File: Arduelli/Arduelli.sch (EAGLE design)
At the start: 2 parts, among them J3 DF12-ELLI-RECEPTABLE-BOTTOM, U1 ARDUINO_SHIELDLONGPADS

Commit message: Preliminary version of Arduelli
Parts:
- removed J3: DF12-ELLI-RECEPTABLE-BOTTOM, ELL-i-Connectors:DF12-ELLI-RECEPTABLE-BOTTOM
- added C1: 10uF, ELL-i-Passives:C0603
- added C10: 33n, ELL-i-Passives:C0402
- added C11, C2, C4, C5, C6, C7, C8, C9: 0.1uF, ELL-i-Passives:C0402
- added C16: 47u, ELL-i-Passives:CPOL6032
- added C17: 47pF, ELL-i-Passives:C0805
- added C39: 100nF, ELL-i-Passives:C0805
- added D1, D4: BAT60J, ell-i:BAT60J
- added D3: MBR120, tinycircuits:AS-ITM-00111
- added FB1, FB2, FB3, FB4: (no value), ELL-i-Passives:FB1206
- added J1, J6: 47346-0001, ELL-i-Connectors:MICRO-USB
- added J2: DF12-ELLI-RECEPTABLE-BOTTOM, ELL-i-Connectors:DF12-ELLI-RECEPTABLE-BOTTOM
- added J4: FTDI-SER-6-PP, ELL-i-Connectors:FTDI-SER-6-PP
- added J5: JTAG_PROG, ELL-i-Connectors:JTAG_PROG
- added Q1: NTZD3152P, ELL-i-DiscreteSemi:NTZD3152P
- added Q2: 2N7002PT, tinycircuits:AS-ITM-00110
- added R1, R11, R12, R13, R2, R20, R21, R22, R3: 100k, ELL-i-Passives:R0402
- added R10, R18, R19, R9: 330, ELL-i-Passives:R0402
- added R14, R15, R16, R17, R4, R6, R7, R8: 24 1%, ELL-i-Passives:R0402
- added R33: 1k5, ELL-i-Passives:R0402
- added R5: 10k, ELL-i-Passives:R0402
- added S1, S3: Push button switch, SparkFun-Electromechanical:SWITCH-MOMENTARY-2SMD
- added S2: EVQQ2/P0, ell-i:EVQQ2/P0
- added SJ16: CLOSED, SparkFun-Passives:SOLDERJUMPERTRACE
- added SJ3, SJ4: OPEN, SparkFun-Passives:SOLDERJUMPERNO
- added SW1, SW2, SW3: (no value), SparkFun-Electromechanical:SW_DIP-2-SMT-HALFSIZE
- added TP2, TP3, TP4: TEST_POINT-5021, ELL-i-Passives:TEST_POINT-5021
- added U2: STM32F103RB, ELL-i-DigitalIC:STM32F103RB
- added U3, U4: ADUM4160BRWZ, ELL-i-PowerIC:ADUM4160BRWZ
- added U5: NCP1117, ell-i:NCP1117
- added X1, X2: XMK-8788K5-BX1X, ELL-i-Connectors:POE-TP-SHIELDED-LEDS
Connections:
- removed net RX+: J3.RX+
- removed net RX-: J3.RX-
- removed net TX+: J3.TX+
- removed net TX-: J3.TX-
- removed net VBAT: J3.VBATT
- removed net VDDA: J3.AREF
- new net +5V0: C16.+, TP2.P$1, U5.OUT, U5.TAB
- new net -RTS: C10.2, SW1.3
- new net AGND: C11.1, C5.1, C6.1, C9.1, S1.2, S3.2, U3.GND2, U3.GND2_2, U4.GND2, U4.GND2_2, X1LED2.C, X2LED2.C
- new net AREF: J2.AREF
- new net BOOT0TX: J4.TXD, R5.1, SW1.4
- new net CTS: J4.-CTS
- new net D14: J2.IO5
- new net D15: J2.MOSI
- new net D16: J2.IO3
- new net D17: J2.IO8
- new net D18: J2.IO2
- new net DDD+: R8.2
- new net DDD-: R7.2
- new net DPIN: U3.PIN
- new net DSPD: U3.SPD
- new net DSPU: U3.SPU
- new net DUD+: J1.D+, R6.1
- new net DUD-: J1.D-, R4.1
- new net DVBUS1: C2.2, FB1.1, R10.2, U3.VBUS1
- new net DVBUS2: R9.1
- new net DVDD1: C4.2, U3.PDEN, U3.VDD1
- new net ETH_INT: J2.ETH_INT/TX+
- new net ETH_RX+: J2.RX+
- new net ETH_RX-: J2.RX-
- new net GND: C1.2, C2.1, C4.1, C7.1, C8.1, FB2.1, FB4.1, J1.P1, J1.P2, J1.P3, J1.P4, J1.P5, J1.P6, J5.3, J5.5, J5.9, J6.P1, J6.P2, J6.P3, J6.P4, J6.P5, J6.P6, Q2.S, R1.1, U3.GND1, U3.GND1_2, U4.GND1, U4.GND1_2, X1LED1.C, X2LED1.C
- new net GNDA: R3.1
- new net HDD+: R17.2, SJ4.2
- new net HDD-: R16.2, SJ3.2
- new net HPIN: U4.PIN
- new net HSPD: U4.SPD
- new net HSPU: U4.SPU
- new net HUD+: J6.D+, R15.1
- new net HUD-: J6.D-, R14.1
- new net HVBUS1: C7.2, R19.2, U4.VBUS1
- new net HVBUS2: FB3.1, R18.1
- new net HVDD1: C8.2, U4.PDEN, U4.VDD1
- new net N$1: FB1.2, J1.VBUS
- new net N$15: C1.1
- new net N$16: R7.1, U3.DD-
- new net N$17: R8.1, U3.DD+
- new net N$18: R11.1
- new net N$19: R12.1
- new net N$2: D3.C, Q1.D2
- new net N$20: R11.2
- new net N$21: R12.2
- new net N$22: R13.1
- new net N$23: R13.2, S1.1
- new net N$24: FB3.2, J6.VBUS
- new net N$25: FB4.2, J6.GND
- new net N$26: R14.2, U4.UD-
- new net N$27: R15.2, U4.UD+
- new net N$28: R16.1, U4.DD-
- new net N$29: R17.1, U4.DD+
- new net N$3: FB2.2, J1.GND
- new net N$30: R18.2, X2LED2.A
- new net N$31: R19.1, X2LED1.A
- new net N$32: R20.1
- new net N$33: R21.1
- new net N$34: R20.2
- new net N$35: C17.1, C39.1, TP3.P$1, U5.IN
- new net N$36: R9.2, X1LED2.A
- new net N$37: R21.2
- new net N$38: R10.1, X1LED1.A
- new net N$39: R22.1
- new net N$4: U2PA.PA11
- new net N$40: R22.2, S3.1
- new net N$5: U2PA.PA12
- new net N$58: C16.-, C17.2, C39.2, TP4.P$1, U5.GND
- new net N$6: R4.2, U3.UD-
- new net N$7: R6.2, U3.UD+
- new net N$8: Q1.G2, Q2.D, R2.1
- new net RSV2: J2.RSV2
- new net RTS: C10.1, J4.-RTS
- new net RX: R5.2, SW3.1, U2PA.PA10
- new net TCLK: J5.4, U2PA.PA5-ADC_IN5
- new net TDI: J5.8, U2PA.PA3-ADC_IN3
- new net TDO: J5.6, U2PA.PA6-ADC_IN6
- new net TMS: J5.2, U2PA.PA4-ADC_IN4
- new net TX: J4.RXD, SW3.2, U2PA.PA9
- new net USB_POWER: Q1.D1, R1.2
- new net VBATT: J2.VBATT
- new net VCC: Q1.S1, Q1.S2, R2.2
- new net VCC-IN: D4.A, J4.VCC
- new net VCCIO: J2.VCC(IO), SJ16.1
- net +3V3: now also C11.2, C5.2, C6.2, C9.2, D1.C, D4.C, J2.3.3V@48, J2.3.3V@6, J2.ETH_MUX, J5.1, SJ16.2, U3.VBUS2, U3.VDD2, U4.VBUS2, U4.VDD2; no longer J3.3.3V@48, J3.3.3V@6, J3.VCC(IO)
- net +5V: now also D3.A, J2.5V, Q1.G1, Q2.G, R3.2; no longer J3.5V
- net A0: now also J2.AD0; no longer J3.AD0
- net A1: now also J2.AD1; no longer J3.AD1
- net A2: now also J2.AD2; no longer J3.AD2
- net A3: now also J2.AD3; no longer J3.AD3
- net A4: now also J2.SDA; no longer J3.SDA
- net A5: now also J2.SCL; no longer J3.SCL
- net BOOT0: now also J2.BOOT0, R33.2, SW1.1, U2PD_CTL.BOOT0; no longer J3.RSV2
- net D0: now also SW3.3, U1.RX; no longer J3.IO0
- net D1: now also SW3.4, U1.TX; no longer J3.IO1
- net D10: now also J2.SS; no longer J3.SS
- net D11: now also J2.SCK; no longer J3.MOSI
- net D12: now also J2.MISO; no longer J3.MISO
- net D13: no longer J3.SCK
- net D2: now also J2.TX1/IO1; no longer J3.IO2
- net D3: now also SJ3.1; no longer J3.IO3
- net D4: now also SJ4.1; no longer J3.IO4
- net D5: now also J2.RX1/IO0; no longer J3.IO5
- net D6: now also J2.IO6; no longer J3.IO6
- net D7: now also J2.IO4; no longer J3.IO7
- net D8: now also J2.IO7; no longer J3.IO8
- net D9: now also J2.IO9; no longer J3.IO9
- net E0: now also J2.E0; no longer J3.E0
- net E1: now also J2.E1; no longer J3.E1
- net E10: now also J2.E10; no longer J3.E10
- net E11: now also J2.E11; no longer J3.E11
- net E12: now also J2.SDA2; no longer J3.SDA2
- net E13: now also J2.SCL2; no longer J3.SCL2
- net E14: now also J2.SS2/CANRX; no longer J3.SS2/CANRX
- net E15: now also J2.MOSI2; no longer J3.MOSI2
- net E16: now also J2.MISO2; no longer J3.MISO2
- net E17: now also J2.SCK2/CANTX; no longer J3.SCK2/CANTX
- net E18: now also J2.RX2/E18; no longer J3.E18
- net E19: now also J2.TX2/E19; no longer J3.E19
- net E2: now also J2.E2; no longer J3.E2
- net E3: now also J2.E3; no longer J3.E3
- net E4: now also J2.E4; no longer J3.E4
- net E5: now also J2.E5; no longer J3.E5
- net E6: now also J2.E6; no longer J3.E6
- net E7: now also J2.E7; no longer J3.E7
- net E8: now also J2.E8; no longer J3.E8
- net E9: now also J2.E9; no longer J3.E9
- net ETH_SS: now also J2.ETH_SS/TX-; no longer J3.ETH_SPI_SS
- net GNDI: now also J2.GND@12, J2.GND@14, J2.GND@46, J4.GND, R33.1, S2.P; no longer J3.ETH_MUX, J3.GND@12, J3.GND@14, J3.GND@46
- net NRES: now also D1.A, J2.-RESET, J5.10, S2.S, SW1.2, U2PD_CTL.NRST; no longer J3.-RESET
- net RSV0: now also J2.RSV0; no longer J3.RSV0
- net RSV1: now also J2.RSV1; no longer J3.RSV1
- net VIN: now also J2.VIN; no longer J3.VIN
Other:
- note added: "Connect close to the package"
- note added: "IO expansion bus"
- note added: "LED indicators for power"
- note added: "Low ESR"
- note added: "POE POWER"
- note added: "Power arbitration"
- note added: "RESET LOGIC"
- note added: "Simulate device disconnect"
- note added: "UGND"
- note added: "USB POWER"
- note added: "USB debug interface"
- note added: "USB2.0 speeds - Pulled up USB1.0 speeds - Pulled down Default - Pulled up"
- note added: "VCC of Ardueli"
- note added: "V_USB"
- moved on the sheet: U1

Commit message: Arduelli with the crystal and other connections
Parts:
- removed SW2: (no value), SparkFun-Electromechanical:SW_DIP-2-SMT-HALFSIZE
- added C12, C3: 18pF, ELL-i-Passives:C0402
- added Q3: 8MHz, SparkFun-FreqCtrl:CRYSTAL_WITH_GND
- added R23: 330E, ELL-i-Passives:R0402
- added SW4: (no value), SparkFun-Electromechanical:SW_DIP-8-SMT-HALFSIZE
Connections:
- removed net N$35: C17.1, C39.1, TP3.P$1, U5.IN
- removed net N$58: C16.-, C17.2, C39.2, TP4.P$1, U5.GND
- new net LDO_GND: C16.-, C17.2, C39.2, SW4.5, SW4.7, TP4.P$1, U5.GND
- new net LDO_IN: C17.1, C39.1, SW4.6, SW4.8, TP3.P$1, U5.IN
- new net N$10: C12.2, Q3.C2, R23.2
- new net N$9: C3.2, Q3.C1, U2PD_CTL.PD0
- net +3V3: now also U2PB.PB4, U2PWR.VBAT, U2PWR.VDD1, U2PWR.VDD2, U2PWR.VDD3, U2PWR.VDD4, U2PWR.VDDA
- net DDD+: now also U2PA.PA12
- net DDD-: now also U2PA.PA11
- net DVBUS1: now also SW4.9
- net GND: now also C12.1, C3.1, SW4.10, U2PWR.VSS1, U2PWR.VSS2, U2PWR.VSS3, U2PWR.VSS4, U2PWR.VSSA
- net GNDI: now also SW4.12
- net HVBUS2: now also SW4.11
- net N$4: now also Q3.GND@1, Q3.GND@2; no longer U2PA.PA11
- net N$5: now also R23.1, U2PD_CTL.PD1; no longer U2PA.PA12
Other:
- moved on the sheet: C1, C10, D1, D3, D4, J4, Q1, Q2, R1, R2, R3, R33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

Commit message: Fixed the RJ45 issue in layout. Minor fixes.
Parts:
- removed Q3: 8MHz, SparkFun-FreqCtrl:CRYSTAL_WITH_GND
- removed R23: 330E, ELL-i-Passives:R0402
- removed X1, X2: XMK-8788K5-BX1X, ELL-i-Connectors:POE-TP-SHIELDED-LEDS
- added D2, D5, D6, D7: GREEN, SparkFun-LED:LED-GREEN0603
- added Y1: 8MHz, SparkFun-FreqCtrl:CRYSTALTXC-7A
- C12, C3: value 18pF -> 16pF
- R10, R18, R19, R9: value 330 -> (none)
- U2: value STM32F103RB -> STM32F103RBT; device ELL-i-DigitalIC:STM32F103RB -> ELL-i-DigitalIC:STM32F103RBT
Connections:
- removed net N$30: R18.2, X2LED2.A
- removed net N$31: R19.1, X2LED1.A
- removed net N$36: R9.2, X1LED2.A
- removed net N$38: R10.1, X1LED1.A
- new net N$11: D2.C, R9.1
- new net N$12: D5.C, R10.1
- net AGND: now also R10.2, R19.2; no longer X1LED2.C, X2LED2.C
- net DVBUS1: now also D2.A; no longer R10.2
- net DVBUS2: now also D5.A; no longer R9.1
- net GND: now also R18.2, R9.2; no longer X1LED1.C, X2LED1.C
- net HVBUS1: now also D6.A; no longer R19.2
- net HVBUS2: now also D7.A; no longer R18.1
- net N$10: now also U2PD_CTL.PD1; no longer Q3.C2, R23.2
- net N$4: now also D6.C, R18.1; no longer Q3.GND@1, Q3.GND@2
- net N$5: now also D7.C, R19.1; no longer R23.1, U2PD_CTL.PD1
- net N$9: no longer Q3.C1
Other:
- moved on the sheet: R10, R18, R19, R9

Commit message: Added pins, nets for Arduino header. Minor fixes.
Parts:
- R10, R18, R19, R9: value (none) -> 150R
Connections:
- removed net D14: J2.IO5
- removed net D15: J2.MOSI
- removed net D16: J2.IO3
- removed net D17: J2.IO8
- removed net D18: J2.IO2
- net +3V3: now also U1.3.3V
- net +5V: now also U1.5V
- net A0: now also U1.A0
- net A1: now also U1.A1
- net A2: now also U1.A2
- net A3: now also U1.A3
- net A4: now also U1.A4
- net A5: now also U1.A5
- net AREF: now also U1.AREF
- net D0: now also J2.RX1/IO0
- net D1: now also J2.TX1/IO1
- net D10: now also U1.*D10
- net D11: now also J2.MOSI, U1.*D11; no longer J2.SCK
- net D12: now also U1.D12
- net D13: now also J2.SCK
- net D2: now also J2.IO2, U1.D2; no longer J2.TX1/IO1
- net D3: now also J2.IO3, U1.*D3
- net D4: now also J2.IO4, U1.D4
- net D5: now also J2.IO5, U1.*D5; no longer J2.RX1/IO0
- net D6: now also U1.*D6
- net D7: now also J2.IO7, U1.D7; no longer J2.IO4
- net D8: now also J2.IO8, U1.D8; no longer J2.IO7
- net D9: now also U1.*D9
- net GND: now also U1.GND@0, U1.GND@1, U1.GND@2
- net NRES: now also U1.RES
- net VIN: now also U1.VIN

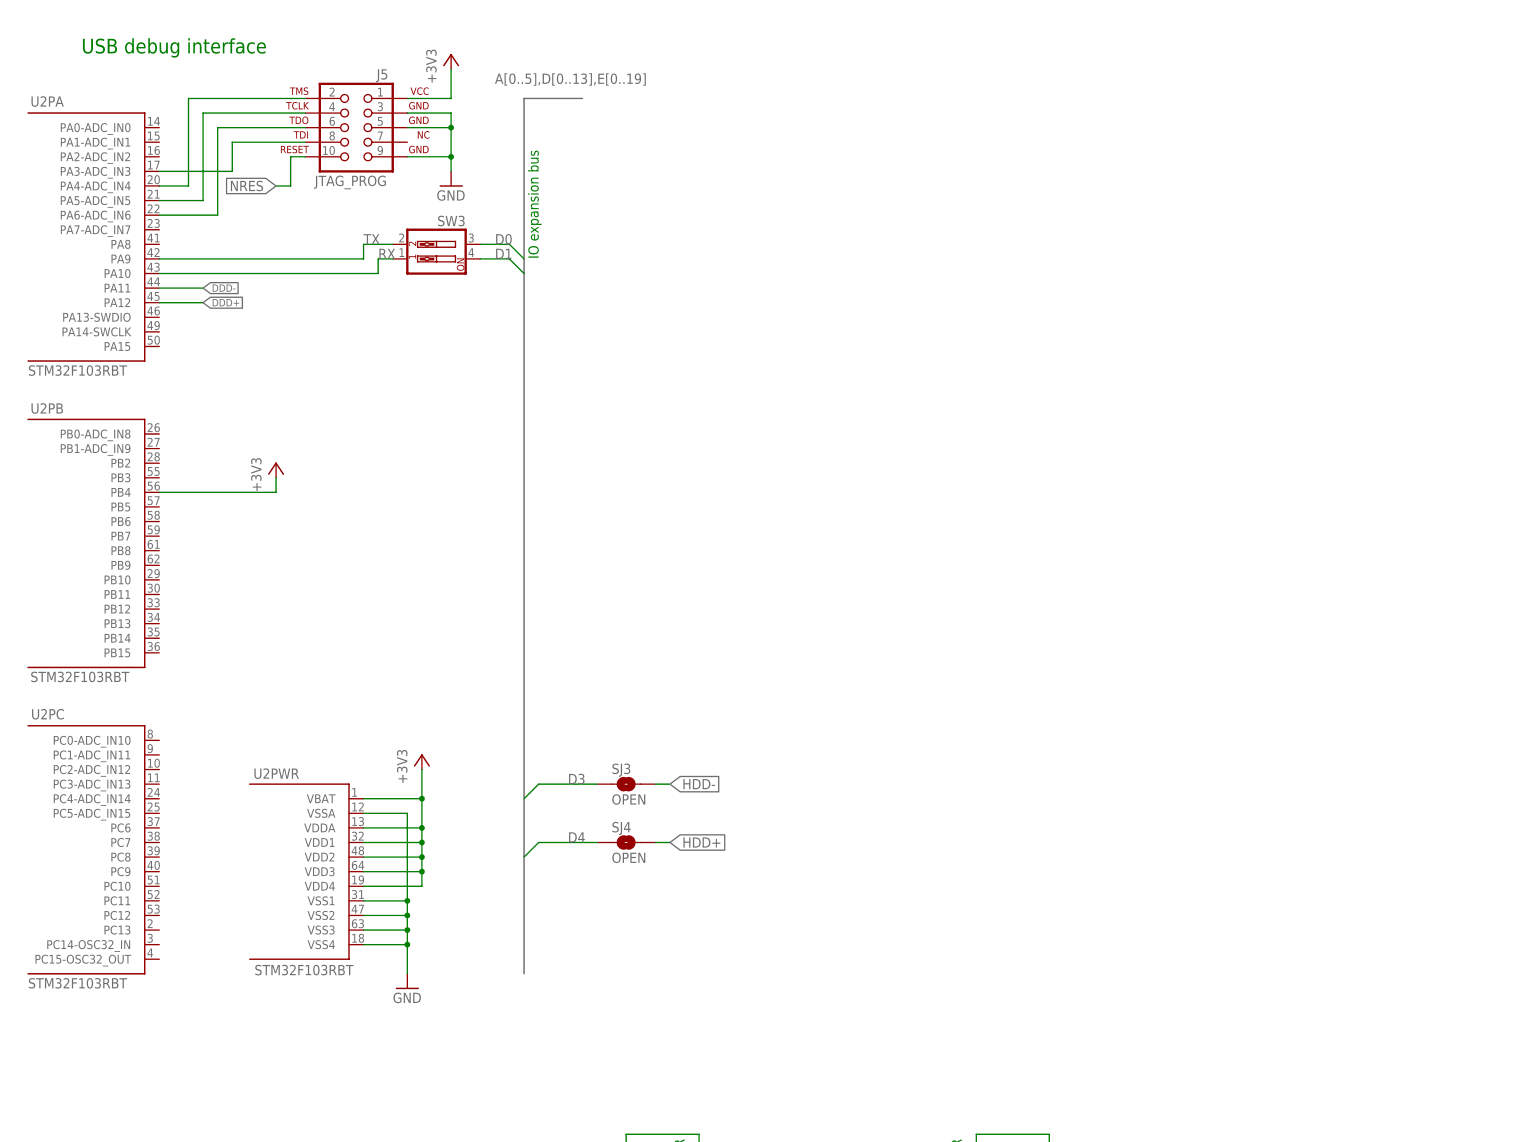
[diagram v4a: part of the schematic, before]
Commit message: Adding connections to the ELL-i bus. Other fixes.
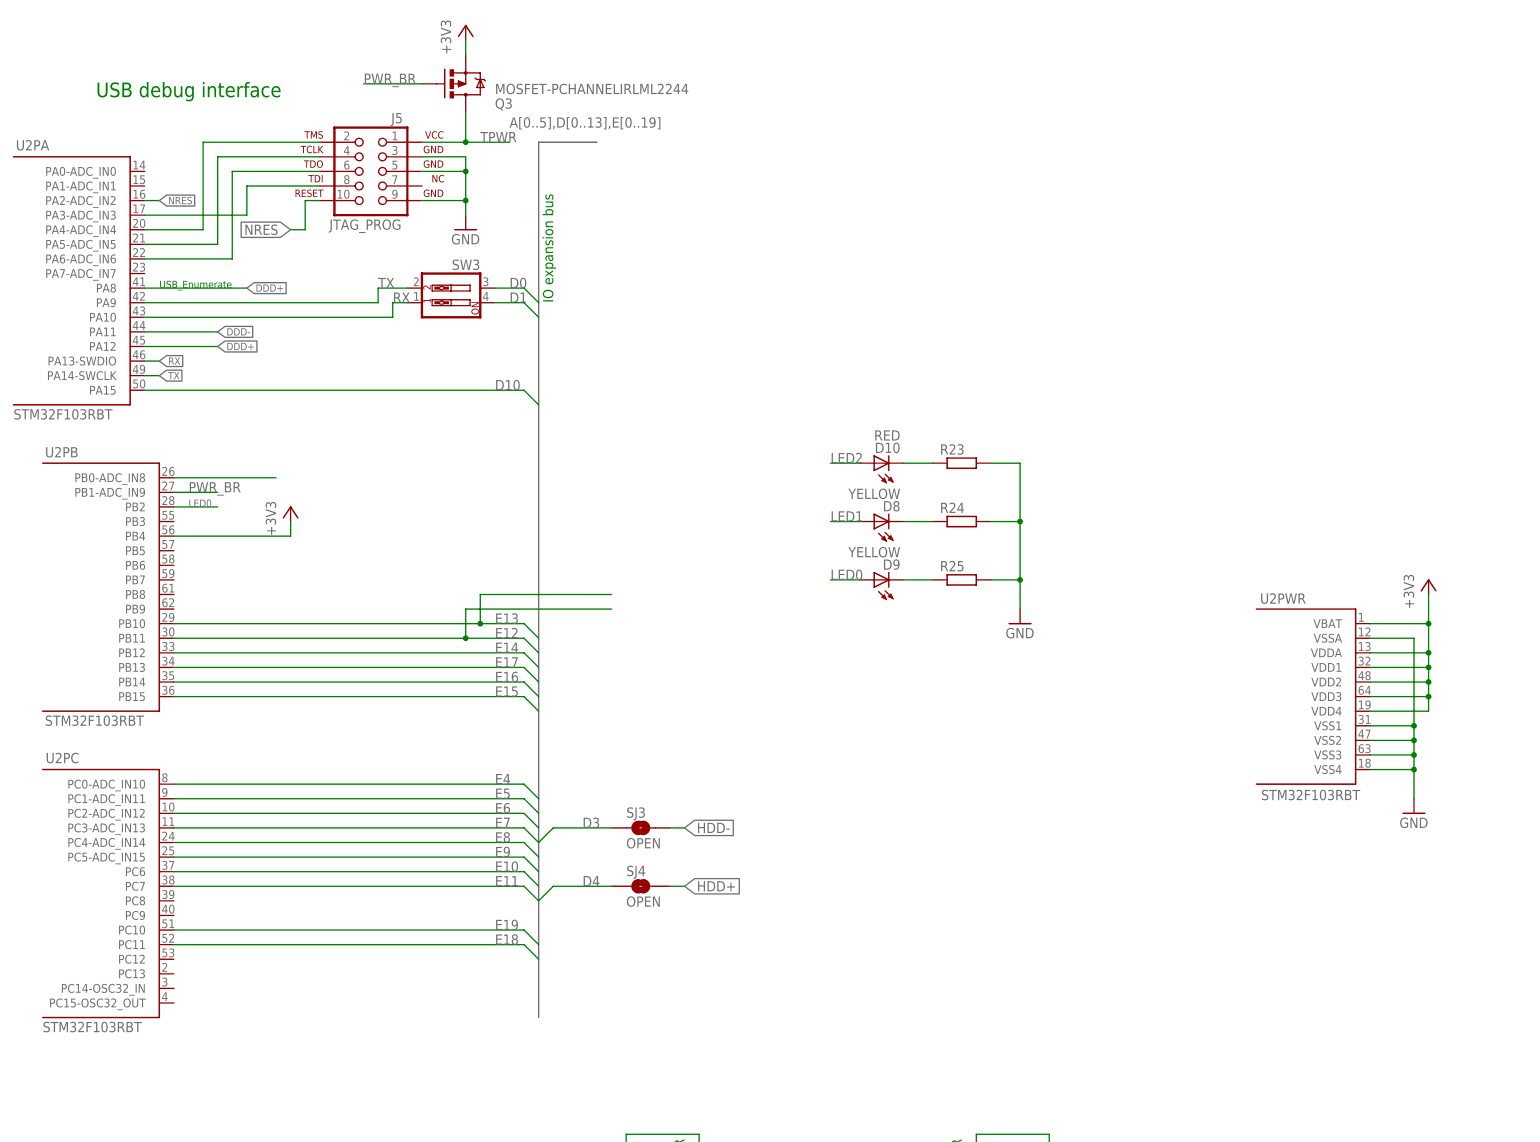
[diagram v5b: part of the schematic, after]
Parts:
- added D10: RED, SparkFun-LED:LED-RED0603
- added D8, D9: YELLOW, SparkFun-LED:LED-YELLOW0603
- added Q3: MOSFET-PCHANNELIRLML2244, SparkFun-DiscreteSemi:MOSFET-PCHANNELIRLML2244
- added R23, R24, R25: (no value), ELL-i-Passives:R0402
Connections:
- new net LED0: D9.A, U2PB.PB2
- new net LED1: D8.A
- new net LED2: D10.A
- new net N$13: D10.C, R23.1
- new net N$14: D8.C, R24.1
- new net N$30: D9.C, R25.1
- new net N$31: U2PB.PB0-ADC_IN8
- new net PWR_BR: Q3.G, U2PB.PB1-ADC_IN9
- new net TPWR: J5.1, Q3.D
- net +3V3: now also Q3.S; no longer J5.1
- net D10: now also U2PA.PA15
- net DDD+: now also U2PA.PA8
- net E10: now also U2PC.PC6
- net E11: now also U2PC.PC7
- net E12: now also U2PB.PB11
- net E13: now also U2PB.PB10
- net E14: now also U2PB.PB12
- net E15: now also U2PB.PB15
- net E16: now also U2PB.PB14
- net E17: now also U2PB.PB13
- net E18: now also U2PC.PC11
- net E19: now also U2PC.PC10
- net E4: now also U2PC.PC0-ADC_IN10
- net E5: now also U2PC.PC1-ADC_IN11
- net E6: now also U2PC.PC2-ADC_IN12
- net E7: now also U2PC.PC3-ADC_IN13
- net E8: now also U2PC.PC4-ADC_IN14
- net E9: now also U2PC.PC5-ADC_IN15
- net GND: now also R23.2, R24.2, R25.2
- net NRES: now also U2PA.PA2-ADC_IN2
- net RX: now also U2PA.PA13-SWDIO
- net TX: now also U2PA.PA14-SWCLK
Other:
- note added: "USB_Enumerate"
- moved on the sheet: J5, SJ3, SJ4, SW3, U2PA, U2PB, U2PC, U2PWR

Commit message: Added M2 screw holes. Connections to the ELL-i bus.
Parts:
- added X1, X2, X3, X4, X5: M-BOLT-2, ELL-i-Connectors:M-BOLT-2
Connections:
- removed net LED1: D8.A
- new net N$35: X5.KL1
- net +3V3: now also X4.KL1
- net AGND: now also C12.1, C3.1, J4.GND, J5.3, J5.5, J5.9, R23.2, R24.2, R25.2, R33.1, S2.P, U2PWR.VSS1, U2PWR.VSS2, U2PWR.VSS3, U2PWR.VSS4, U2PWR.VSSA, X2.KL1; no longer C11.1, C9.1, R19.2, S3.2, U4.GND2, U4.GND2_2
- net E12: now also D9.A
- net E13: now also D8.A
- net GND: now also X1.KL1; no longer C12.1, C3.1, J5.3, J5.5, J5.9, R23.2, R24.2, R25.2, U2PWR.VSS1, U2PWR.VSS2, U2PWR.VSS3, U2PWR.VSS4, U2PWR.VSSA
- net GNDI: now also C11.1, C9.1, R19.2, S3.2, U4.GND2, U4.GND2_2, X3.KL1; no longer J4.GND, R33.1, S2.P
- net LED0: no longer D9.A
- net N$10: now also Y1.2
- net N$9: now also Y1.1
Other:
- moved on the sheet: C10, C12, C3, D1, D10, D4, D8, D9, J4, R23, R24, R25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

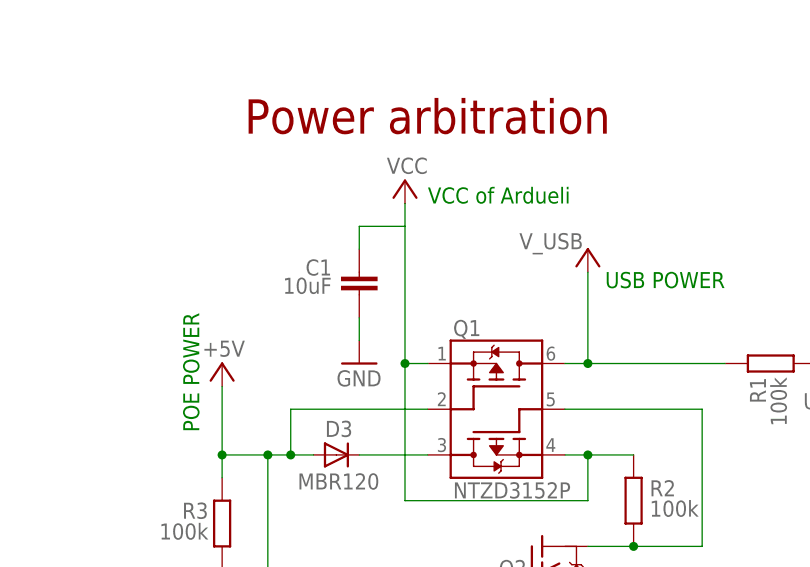
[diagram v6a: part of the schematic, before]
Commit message: Added Junction to the Power arbitration circuit
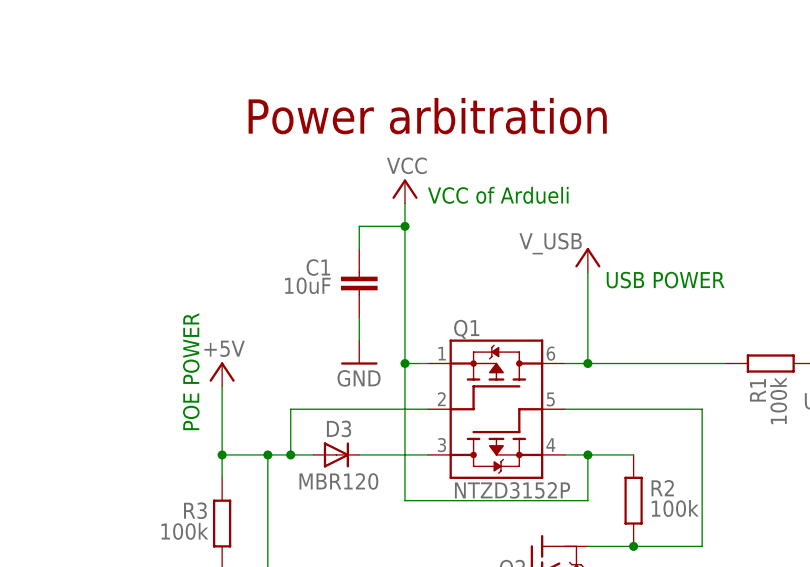
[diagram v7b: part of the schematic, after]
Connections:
- removed net N$15: C1.1
- net VCC: now also C1.1
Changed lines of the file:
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@@
-</segment>
-</net>
-<net name="N$15" class="0">
-<segment>
-<wire x1="215.9" y1="-106.68" x2="220.98" y2="-106.68" width="0.1524" layer="91"/>
-<pinref part="C1" gate="G$1" pin="1"/>
-<wire x1="215.9" y1="-109.22" x2="215.9" y2="-106.68" width="0.1524" layer="91"/>
 </segment>
 </net>
@@
 <wire x1="223.52" y1="-121.92" x2="220.98" y2="-121.92" width="0.1524" layer="91"/>
 <pinref part="VCC" gate="VCC" pin="VCC"/>
-<wire x1="220.98" y1="-104.14" x2="220.98" y2="-121.92" width="0.1524" layer="91"/>
+<wire x1="220.98" y1="-104.14" x2="220.98" y2="-106.68" width="0.1524" layer="91"/>
 <pinref part="R2" gate="G$1" pin="2"/>
 <pinref part="Q1" gate="G$1" pin="S2"/>
+<wire x1="220.98" y1="-106.68" x2="220.98" y2="-121.92" width="0.1524" layer="91"/>
 <wire x1="246.38" y1="-132.08" x2="241.3" y2="-132.08" width="0.1524" layer="91"/>
 <wire x1="241.3" y1="-132.08" x2="238.76" y2="-132.08" width="0.1524" layer="91"/>
@@
 <wire x1="220.98" y1="-137.16" x2="220.98" y2="-121.92" width="0.1524" layer="91"/>
 <junction x="220.98" y="-121.92"/>
+<pinref part="C1" gate="G$1" pin="1"/>
+<wire x1="215.9" y1="-109.22" x2="215.9" y2="-106.68" width="0.1524" layer="91"/>
+<wire x1="215.9" y1="-106.68" x2="220.98" y2="-106.68" width="0.1524" layer="91"/>
+<junction x="220.98" y="-106.68"/>
 </segment>
 </net>
